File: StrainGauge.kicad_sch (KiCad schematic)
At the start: 31 parts, among them J1 Conn_01x04, J2 Conn_01x04, U1 INA333xxDGK, U2 REF2025, U3 OPA310xDBV

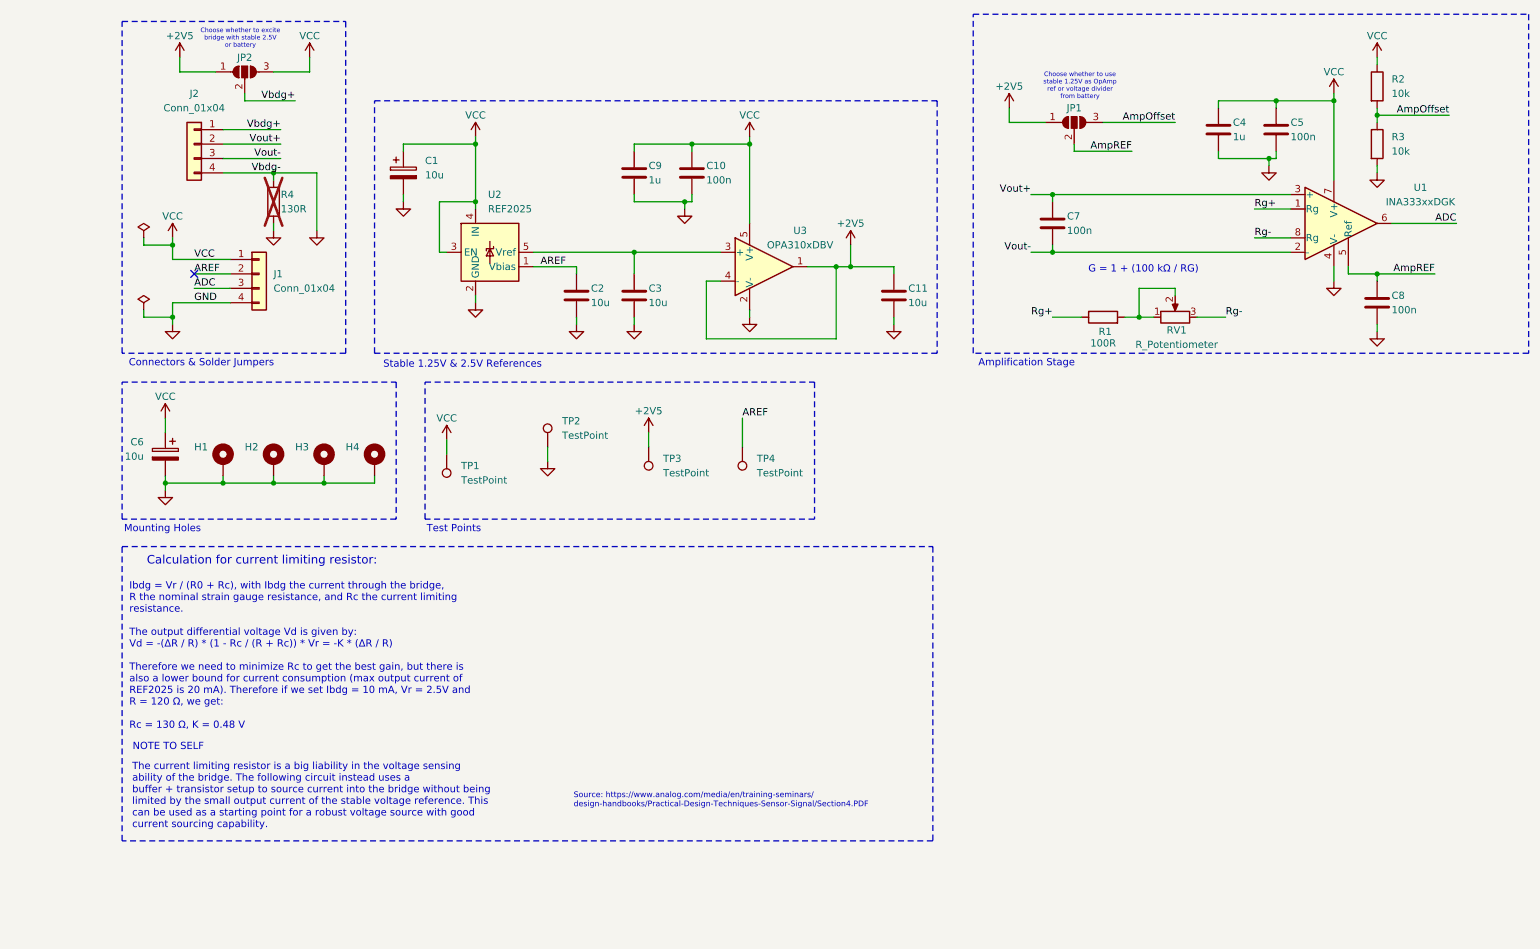
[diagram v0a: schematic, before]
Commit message: added buffer on Ref pin of INA333 (very important), added components list and mostly cleanup
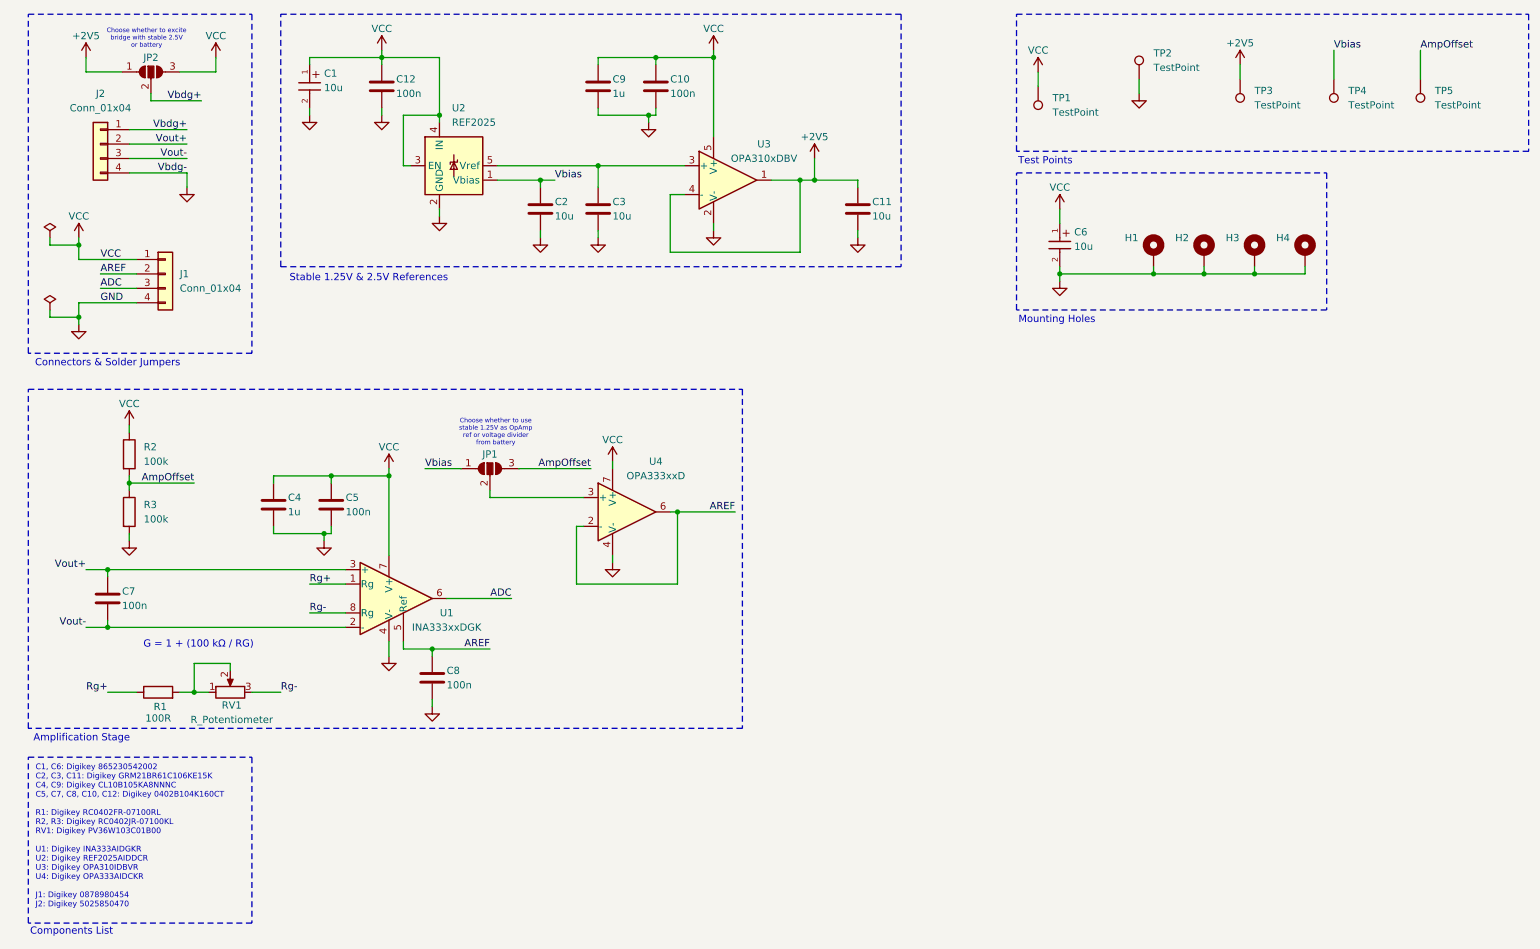
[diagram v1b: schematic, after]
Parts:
- removed C1, C6: 10u, Capacitor_SMD:C_0805_2012Metric, symbol Device:C_Polarized
- removed R4: 130R, Resistor_SMD:R_0402_1005Metric, symbol Device:R
- added C1, C6: 10u, 865230542002:WCAP-AS5H_5X5.5_DXL_, symbol 865230542002:WCAP-AS5H_5X5.5
- added C12: 100n, Capacitor_SMD:C_0402_1005Metric, symbol Device:C
- added TP5: TestPoint, TestPoint:TestPoint_Plated_Hole_D2.0mm, symbol Connector:TestPoint
- added U4: OPA333xxD, Package_SO:SOIC-8_3.9x4.9mm_P1.27mm, symbol Amplifier_Operational:OPA333xxD
- R2, R3: value 10k -> 100k
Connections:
- net +2V5: no longer JP1.1 (A)
- net AREF: now also C8.1, U1.5 (Ref), U4.2 (-), U4.6; no longer C2.1, TP4.1, U2.1 (Vbias)
- net AmpOffset: now also TP5.1
- net GND: now also C1.2, C12.2, C6.2, U4.4 (V-)
- net VCC: now also C1.1, C12.1, C6.1, U4.7 (V+)
- removed net AmpREF: C8.1, JP1.2 (C), U1.5 (Ref)
- new net: JP1.2 (C), U4.3 (+)
- new net Vbias: C2.1, JP1.1 (A), TP4.1, U2.1 (Vbias)
- no-connect marks 1 -> 0
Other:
- note added: "C1, C6: Digikey 865230542002 C2, C3, C11: Digikey GRM21BR61C106KE15K C4, C9: Digikey CL10B105KA8NNNC C5, C7, C8, C10, C12: Digikey 0402B104K160CT R1: Digikey RC0402FR-07100RL R2, R3: Digikey RC0402JR-07100KL RV1: Digikey PV36W103C01B00 U1: Digikey INA333AIDGKR U2: Digikey REF2025AIDDCR U3: Digikey OPA310IDBVR U4: Digikey OPA333AIDCKR J1: Digikey 0878980454 J2: Digikey 5025850470"
- note added: "Components List"
- note removed: "Calculation for current limiting resistor:"
- note removed: "Ibdg = Vr / (R0 + Rc), with Ibdg the current through the bridge, R the nominal strain gauge resistance, and Rc the current limiting resistance. The output differential voltage Vd is given by: Vd = -(ΔR / R) * (1 - Rc / (R + Rc)) * Vr = -K * (ΔR / R) Therefore we need to minimize Rc to get the best gain, but there is also a lower bound for current consumption (max output current of REF2025 is 20 m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"
- note removed: "NOTE TO SELF"
- note removed: "Source: https://www.analog.com/media/en/training-seminars/ design-handbooks/Practical-Design-Techniques-Sensor-Signal/Section4.PDF"
- note removed: "The current limiting resistor is a big liability in the voltage sensing ability of the bridge. The following circuit instead uses a buffer + transistor setup to source current into the bridge without being limited by the small output current of the stable voltage reference. This can be used as a starting point for a robust voltage source with good current sourcing capability."
- moved on the sheet: C10, C11, C2, C3, C4, C5, C7, C8, C9, H1, H2, H3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

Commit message: first spice simulations, step models for components and first version of PCB
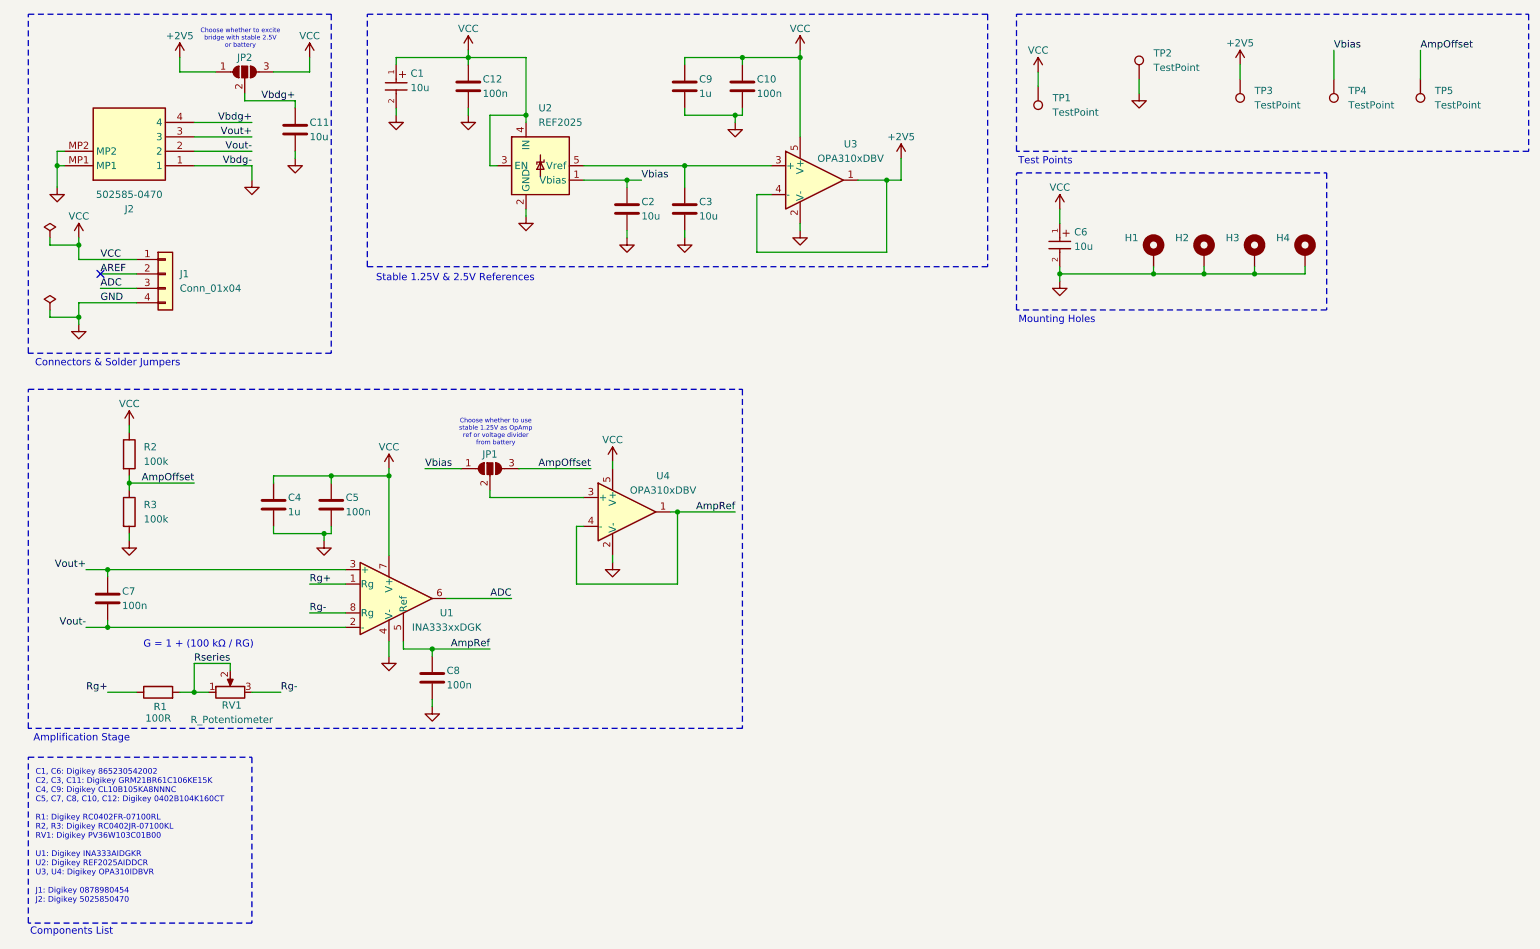
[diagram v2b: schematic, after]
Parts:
- removed J2: Conn_01x04, CLIK-Mate 502585:5025850470, symbol Connector_Generic:Conn_01x04
- removed U4: OPA333xxD, Package_SO:SOIC-8_3.9x4.9mm_P1.27mm, symbol Amplifier_Operational:OPA333xxD
- added J2: 502585-0470, CLIK-Mate 502585:5025850470, symbol CLIK-Mate 502585:502585-0470
- added U4: OPA310xDBV, Package_TO_SOT_SMD:SOT-23-5, symbol Amplifier_Operational:OPA310xDBV
- RV1: footprint PV36W103C01B00:TRIM_PV36W103C01B00 -> PV36W103C01B00:RES3_PV36W103C01B00_BRN
- TP1, TP2, TP3, TP4, TP5: footprint TestPoint:TestPoint_Plated_Hole_D2.0mm -> TestPoint:TestPoint_Pad_2.0x2.0mm
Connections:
- net +2V5: no longer C11.1
- net AREF: no longer C8.1, U1.5 (Ref)
- net GND: now also J2.1, J2.MP1, J2.MP2, U4.2 (V-)
- net VCC: now also U4.5 (V+)
- net Vbdg+: now also C11.1, J2.4
- net Vout+: now also J2.3
- net Vout-: now also J2.2
- net at JP1.2 (C): now also U4.3 (+)
- net Rseries: now reaches R1.2, RV1.1, RV1.2
- new net AmpRef: C8.1, U1.5 (Ref), U4.1, U4.4 (-)
- no-connect marks 0 -> 1
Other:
- note added: "C1, C6: Digikey 865230542002 C2, C3, C11: Digikey GRM21BR61C106KE15K C4, C9: Digikey CL10B105KA8NNNC C5, C7, C8, C10, C12: Digikey 0402B104K160CT R1: Digikey RC0402FR-07100RL R2, R3: Digikey RC0402JR-07100KL RV1: Digikey PV36W103C01B00 U1: Digikey INA333AIDGKR U2: Digikey REF2025AIDDCR U3, U4: Digikey OPA310IDBVR J1: Digikey 0878980454 J2: Digikey 5025850470"
- note removed: "C1, C6: Digikey 865230542002 C2, C3, C11: Digikey GRM21BR61C106KE15K C4, C9: Digikey CL10B105KA8NNNC C5, C7, C8, C10, C12: Digikey 0402B104K160CT R1: Digikey RC0402FR-07100RL R2, R3: Digikey RC0402JR-07100KL RV1: Digikey PV36W103C01B00 U1: Digikey INA333AIDGKR U2: Digikey REF2025AIDDCR U3: Digikey OPA310IDBVR U4: Digikey OPA333AIDCKR J1: Digikey 0878980454 J2: Digikey 5025850470"
- moved on the sheet: C10, C12, C2, C3, C9, JP2, U2, U3

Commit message: added gerbers
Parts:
- added JP3: SolderJumper_2_Open, Jumper:SolderJumper-2_P1.3mm_Open_RoundedPad1.0x1.5mm, symbol Jumper:SolderJumper_2_Open
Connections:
- net AREF: now also JP3.1 (A)
- net AmpRef: now also JP3.2 (B)
- no-connect marks 1 -> 0
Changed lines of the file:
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@@
 		(color 0 0 0 0)
 	)
-	(no_connect
-		(at 29.21 73.66)
-	)
 	(wire
 		(pts
@@
 	(wire
 		(pts
+			(xy 19.05 38.1) (xy 24.13 38.1)
+		)
+		(stroke
+			(width 0)
+			(type default)
+		)
+	)
+	(wire
+		(pts
 			(xy 59.69 119.38) (xy 68.58 119.38)
 		)
@@
 		(pts
 			(xy 80.01 138.43) (xy 80.01 140.97)
+		)
+		(stroke
+			(width 0)
+			(type default)
+		)
+	)
+	(wire
+		(pts
+			(xy 38.1 38.1) (xy 31.75 38.1)
 		)
 		(stroke
@@
 	(label "Rg+"
 		(at 66.04 128.27 0)
+		(fields_autoplaced yes)
+		(effects
+			(font
+				(size 1.27 1.27)
+			)
+			(justify left bottom)
+		)
+	)
+	(label "AmpRef"
+		(at 38.1 38.1 180)
+		(fields_autoplaced yes)
+		(effects
+			(font
+				(size 1.27 1.27)
+			)
+			(justify right bottom)
+		)
+	)
+	(label "AREF"
+		(at 19.05 38.1 0)
 		(fields_autoplaced yes)
 		(effects
@@
 					(unit 1)
 				)
+			)
+		)
+	)
+	(symbol
+		(lib_id "Jumper:SolderJumper_2_Open")
+		(at 27.94 38.1 0)
+		(unit 1)
+		(exclude_from_sim yes)
+		(in_bom no)
+		(on_board yes)
+		(dnp no)
+		(property "Reference" "JP3"
+			(at 27.94 35.56 0)
+			(effects
+				(font
+					(size 1.27 1.27)
+				)
+			)
+		)
+		(property "Value" "SolderJumper_2_Open"
+			(at 27.94 34.29 0)
+			(effects
+				(font
+					(size 1.27 1.27)
+				)
+				(hide yes)
+			)
+		)
+		(property "Footprint" "Jumper:SolderJumper-2_P1.3mm_Open_RoundedPad1.0x1.5mm"
+			(at 27.94 38.1 0)
+			(effects
+				(font
+					(size 1.27 1.27)
+				)
+				(hide yes)
+			)
+		)
+		(property "Datasheet" "~"
+			(at 27.94 38.1 0)
+			(effects
+				(font
+					(size 1.27 1.27)
+				)
+				(hide yes)
+			)
+		)
+		(property "Description" "Solder Jumper, 2-pole, open"
+			(at 27.94 38.1 0)
+			(effects
+				(font
+					(size 1.27 1.27)
+				)
+				(hide yes)
+			)
+		)
+		(pin "2"
+		)
+		(pin "1"
+		)
+		(instances
+			(project ""
+				(path "/1c58ffeb-c530-4561-bcfa-51e04fb88036"
+					(reference "JP3")
+					(unit 1)
+				)

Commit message: small fixes
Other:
- note added: "C1, C6: Digikey 865230542002 C2, C3, C11: Digikey GRM21BR61C106KE15K C4, C9: Digikey CL10B105KA8NNNC C5, C7, C8, C10, C12: Digikey 0402B104K160CT R1: Digikey RC0402FR-07100RL R2, R3: Digikey RC0402JR-07100KL RV1: Digikey PV36W103C01B00 U1: Digikey INA333AIDGKR U2: Digikey REF2025AIDDCR U3, U4: Digikey OPA310IDBVR J1: Digikey 0878980454 J2: Digikey 5025850470, Digikey 5025780400 (mating connector)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"
- note removed: "C1, C6: Digikey 865230542002 C2, C3, C11: Digikey GRM21BR61C106KE15K C4, C9: Digikey CL10B105KA8NNNC C5, C7, C8, C10, C12: Digikey 0402B104K160CT R1: Digikey RC0402FR-07100RL R2, R3: Digikey RC0402JR-07100KL RV1: Digikey PV36W103C01B00 U1: Digikey INA333AIDGKR U2: Digikey REF2025AIDDCR U3, U4: Digikey OPA310IDBVR J1: Digikey 0878980454 J2: Digikey 5025850470"
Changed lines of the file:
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@@
 	(rectangle
 		(start 16.51 158.75)
-		(end 55.88 187.96)
+		(end 93.98 187.96)
 		(stroke
 			(width 0)
@@
 		)
 	)
-	(text "C1, C6: Digikey 865230542002\nC2, C3, C11: Digikey GRM21BR61C106KE15K\nC4, C9: Digikey CL10B105KA8NNNC\nC5, C7, C8, C10, C12: Digikey 0402B104K160CT\n\nR1: Digikey RC0402FR-07100RL\nR2, R3: Digikey RC0402JR-07100KL\nRV1: Digikey PV36W103C01B00\n\nU1: Digikey INA333AIDGKR\nU2: Digikey REF2025AIDDCR\nU3, U4: Digikey OPA310IDBVR\n\nJ1: Digikey 0878980454\nJ2: Digikey 5025850470"
+	(text "C1, C6: Digikey 865230542002\nC2, C3, C11: Digikey GRM21BR61C106KE15K\nC4, C9: Digikey CL10B105KA8NNNC\nC5, C7, C8, C10, C12: Digikey 0402B104K160CT\n\nR1: Digikey RC0402FR-07100RL\nR2, R3: Digikey RC0402JR-07100KL\nRV1: Digikey PV36W103C01B00\n\nU1: Digikey INA333AIDGKR\nU2: Digikey REF2025AIDDCR\nU3, U4: Digikey OPA310IDBVR\n\nJ1: Digikey 0878980454\nJ2: Digikey 5025850470, Digikey 5025780400 (mating connector), Digikey 5025790000 (crimps)"
 		(exclude_from_sim no)
 		(at 17.78 172.72 0)
